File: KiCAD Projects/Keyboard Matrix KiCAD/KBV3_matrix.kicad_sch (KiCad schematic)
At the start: 100 parts, among them J1 Conn_01x06, U2 TCA8418RTWR

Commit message: Added a parts list summary with current prices for easier BOM Assembly
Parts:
- added J2: Conn_01x10_Socket, Connector_FFC-FPC:Molex_200528-0100_1x10-1MP_P1.00mm_Horizontal, symbol Connector:Conn_01x10_Socket

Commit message: Added RGB LED to the keypad matrix
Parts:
- removed J1: Conn_01x06, symbol Connector_Generic:Conn_01x06
- added C3: 0.1uF, symbol Device:C_Polarized_Small_US
- added LED1, LED10, LED11, LED12, LED13, LED14, LED15, LED16, LED17, LED18, LED19, LED2, LED20, LED21, LED22, LED23, LED24, LED25, LED26, LED27, LED28, LED29, LED3, LED30, LED31, LED32, LED33, LED34, LED35, LED36, LED37, LED38, LED39, LED4, LED40, LED41, LED42, LED43, LED44, LED45, LED46, LED47, LED48, LED5, LED6, LED7, LED8, LED9: PI554FCH, LED_SMD:LED_Inolux_IN-PI554FCH_PLCC4_5.0x5.0mm_P3.2mm, symbol LED:Inolux_IN-PI554FCH
- added R1: 500, symbol Device:R_US
- added R2: 10k, symbol Device:R_US
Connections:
- net +3.3V: now also J2.2 (Pin_2)
- net GND: now also J2.10 (Pin_10), C3.2, LED1.1 (VSS), LED10.1 (VSS), LED11.1 (VSS), LED12.1 (VSS), LED13.1 (VSS), LED14.1 (VSS), LED15.1 (VSS), LED16.1 (VSS), LED17.1 (VSS), LED18.1 (VSS), LED19.1 (VSS), LED2.1 (VSS), LED20.1 (VSS), LED21.1 (VSS), LED22.1 (VSS), LED23.1 (VSS), LED24.1 (VSS), LED25.1 (VSS), LED26.1 (VSS), LED27.1 (VSS), LED28.1 (VSS), LED29.1 (VSS), LED3.1 (VSS), LED30.1 (VSS), LED31.1 (VSS), LED32.1 (VSS), LED33.1 (VSS), LED34.1 (VSS), LED35.1 (VSS), LED36.1 (VSS), LED37.1 (VSS), LED38.1 (VSS), LED39.1 (VSS), LED4.1 (VSS), LED40.1 (VSS), LED41.1 (VSS), LED42.1 (VSS), LED43.1 (VSS), LED44.1 (VSS), LED45.1 (VSS), LED46.1 (VSS), LED47.1 (VSS), LED48.1 (VSS), LED5.1 (VSS), LED6.1 (VSS), LED7.1 (VSS), LED8.1 (VSS), LED9.1 (VSS), R2.2
- net INTn: now also J2.5 (Pin_5)
- net RESETn: now also J2.6 (Pin_6)
- net SCL: now also J2.3 (Pin_3)
- net SDA: now also J2.4 (Pin_4)
- net +5V: now reaches J2.1 (Pin_1)
- net +5V: now also C3.1, LED1.3 (VDD), LED10.3 (VDD), LED11.3 (VDD), LED12.3 (VDD), LED13.3 (VDD), LED14.3 (VDD), LED15.3 (VDD), LED16.3 (VDD), LED17.3 (VDD), LED18.3 (VDD), LED19.3 (VDD), LED2.3 (VDD), LED20.3 (VDD), LED21.3 (VDD), LED22.3 (VDD), LED23.3 (VDD), LED24.3 (VDD), LED25.3 (VDD), LED26.3 (VDD), LED27.3 (VDD), LED28.3 (VDD), LED29.3 (VDD), LED3.3 (VDD), LED30.3 (VDD), LED31.3 (VDD), LED32.3 (VDD), LED33.3 (VDD), LED34.3 (VDD), LED35.3 (VDD), LED36.3 (VDD), LED37.3 (VDD), LED38.3 (VDD), LED39.3 (VDD), LED4.3 (VDD), LED40.3 (VDD), LED41.3 (VDD), LED42.3 (VDD), LED43.3 (VDD), LED44.3 (VDD), LED45.3 (VDD), LED46.3 (VDD), LED47.3 (VDD), LED48.3 (VDD), LED5.3 (VDD), LED6.3 (VDD), LED7.3 (VDD), LED8.3 (VDD), LED9.3 (VDD)
- net LED Din: now reaches J2.8 (Pin_8)
- net LED Din: now also R1.1
- new net: LED37.4 (DO), LED38.2 (DIN)
- new net: LED16.4 (DO), LED17.2 (DIN)
- new net: LED17.4 (DO), LED18.2 (DIN)
- new net: LED29.4 (DO), LED30.2 (DIN)
- new net: LED30.4 (DO), LED31.2 (DIN)
- new net: LED10.4 (DO), LED11.2 (DIN)
- new net: LED11.4 (DO), LED12.2 (DIN)
- new net: LED13.4 (DO), LED14.2 (DIN)
- new net: LED14.4 (DO), LED15.2 (DIN)
- new net: LED4.4 (DO), LED5.2 (DIN)
- new net: LED5.4 (DO), LED6.2 (DIN)
- new net: LED15.4 (DO), LED16.2 (DIN)
- new net: LED48.4 (DO), R2.1
- new net: LED33.4 (DO), LED34.2 (DIN)
- new net: LED34.4 (DO), LED35.2 (DIN)
- new net: LED42.4 (DO), LED43.2 (DIN)
- new net: LED43.4 (DO), LED44.2 (DIN)
- new net: LED2.4 (DO), LED3.2 (DIN)
- new net: LED3.4 (DO), LED4.2 (DIN)
- new net: LED35.4 (DO), LED36.2 (DIN)
- new net: LED38.4 (DO), LED39.2 (DIN)
- new net: LED39.4 (DO), LED40.2 (DIN)
- new net: LED23.4 (DO), LED24.2 (DIN)
- new net: LED47.4 (DO), LED48.2 (DIN)
- new net: LED6.4 (DO), LED7.2 (DIN)
- new net: LED7.4 (DO), LED8.2 (DIN)
- new net: LED46.4 (DO), LED47.2 (DIN)
- new net: LED32.4 (DO), LED33.2 (DIN)
- new net: LED31.4 (DO), LED32.2 (DIN)
- new net: LED20.4 (DO), LED21.2 (DIN)
- new net: LED21.4 (DO), LED22.2 (DIN)
- new net: LED22.4 (DO), LED23.2 (DIN)
- new net: LED25.4 (DO), LED26.2 (DIN)
- new net: LED8.4 (DO), LED9.2 (DIN)
- new net: LED26.4 (DO), LED27.2 (DIN)
- new net: LED27.4 (DO), LED28.2 (DIN)
- new net: LED41.4 (DO), LED42.2 (DIN)
- new net: LED1.2 (DIN), R1.2
- new net: LED1.4 (DO), LED2.2 (DIN)
- new net: LED28.4 (DO), LED29.2 (DIN)
- new net: LED18.4 (DO), LED19.2 (DIN)
- new net: LED44.4 (DO), LED45.2 (DIN)
- new net: LED40.4 (DO), LED41.2 (DIN)
- new net: LED45.4 (DO), LED46.2 (DIN)
- new net: LED19.4 (DO), LED20.2 (DIN)
- new net: LED10.2 (DIN), LED9.4 (DO)
- new net LED Din R2: LED12.4 (DO), LED13.2 (DIN)
- new net LED Din R3: LED24.4 (DO), LED25.2 (DIN)
- new net LED Din R4: LED36.4 (DO), LED37.2 (DIN)
- no-connect marks 2 -> 0
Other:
- moved on the sheet: J2

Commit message: Clean Libraries, Added Datasheet, LDO, etc
Cleaned up some of the footprints that are not needed. Added components for PD and voltage regulation. Only minor changes to schematic
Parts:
- added H1, H2, H3, H4: MountingHole_Pad, symbol Mechanical:MountingHole_Pad
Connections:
- net GND: now also H1.1, H2.1, H3.1, H4.1

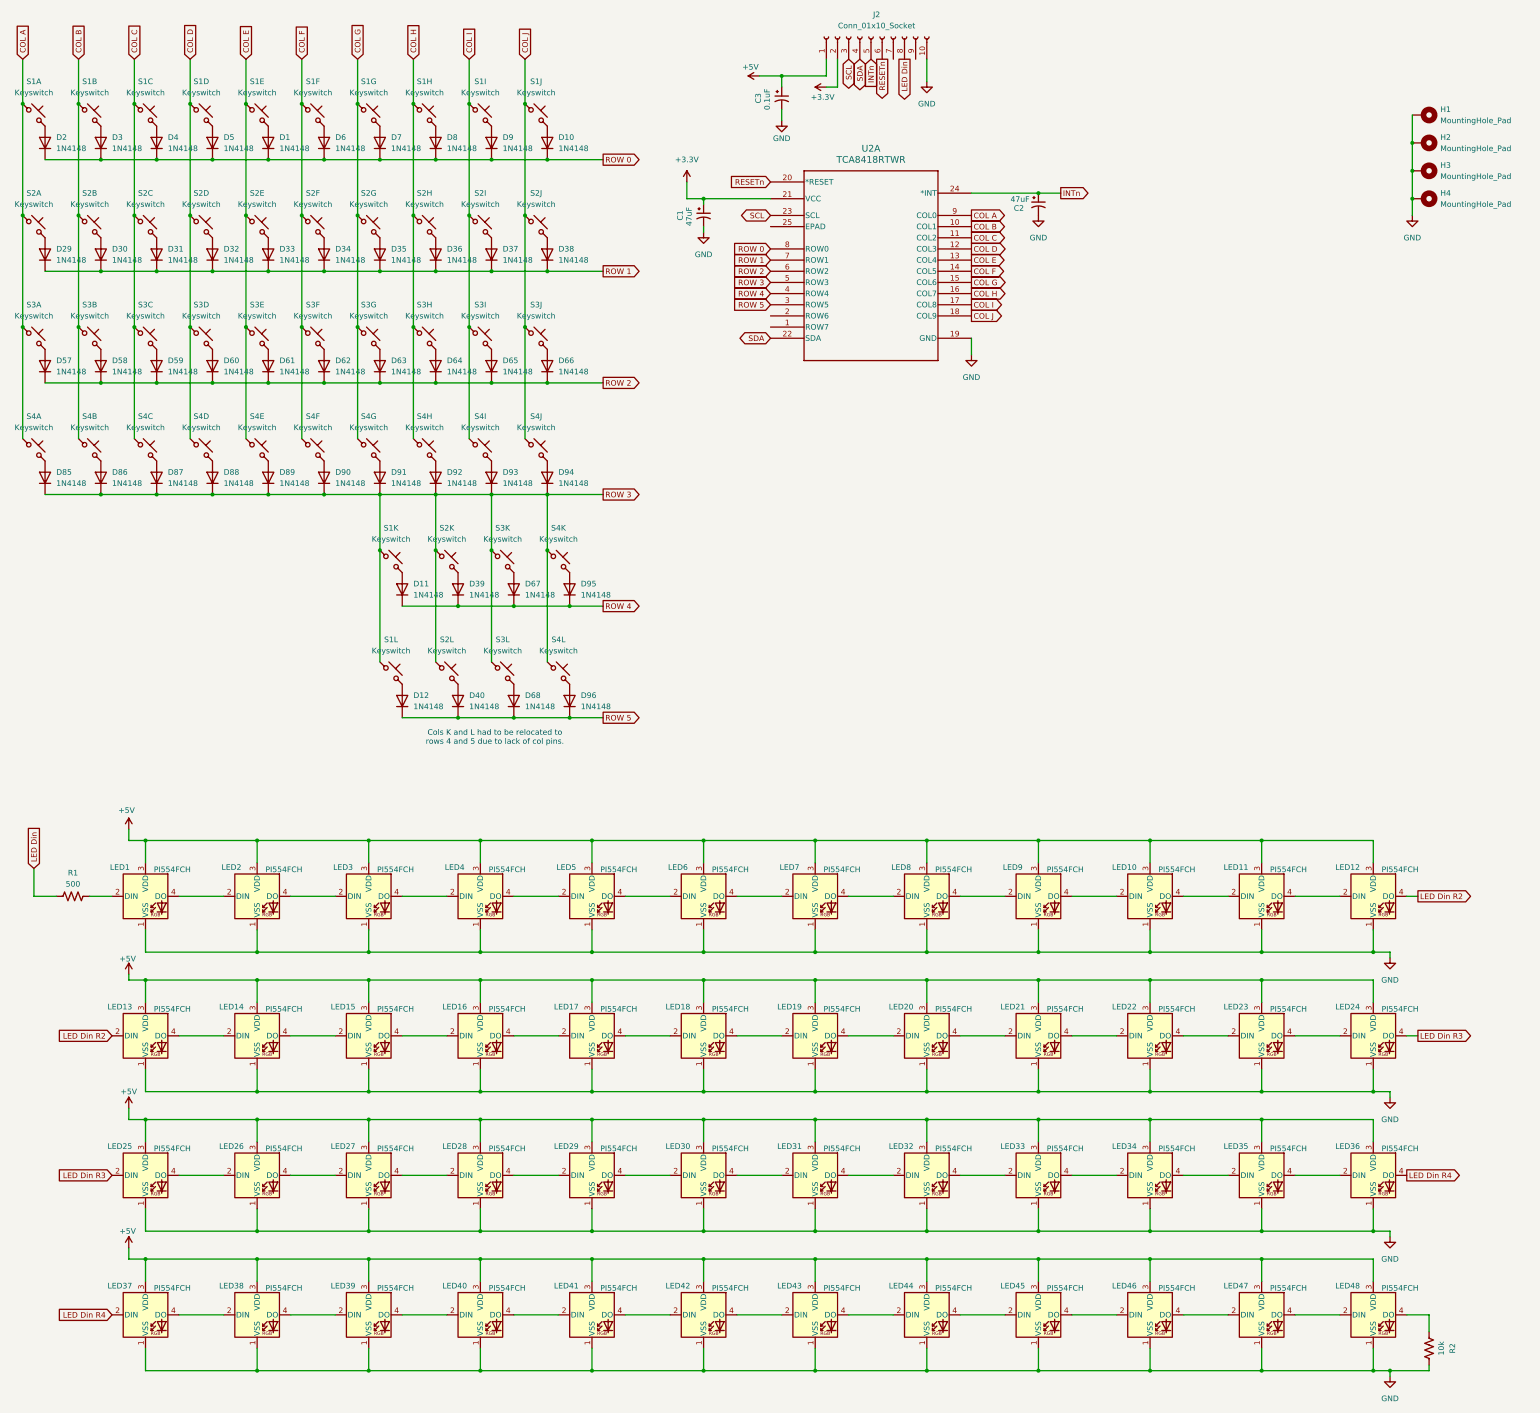
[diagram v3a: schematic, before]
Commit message: Changed the key matrix to one row 6 instead of two smaller rows.  Added USB ESD protection
Changed the key matrix to one row 6 instead of two smaller rows.

Added USB ESD protection
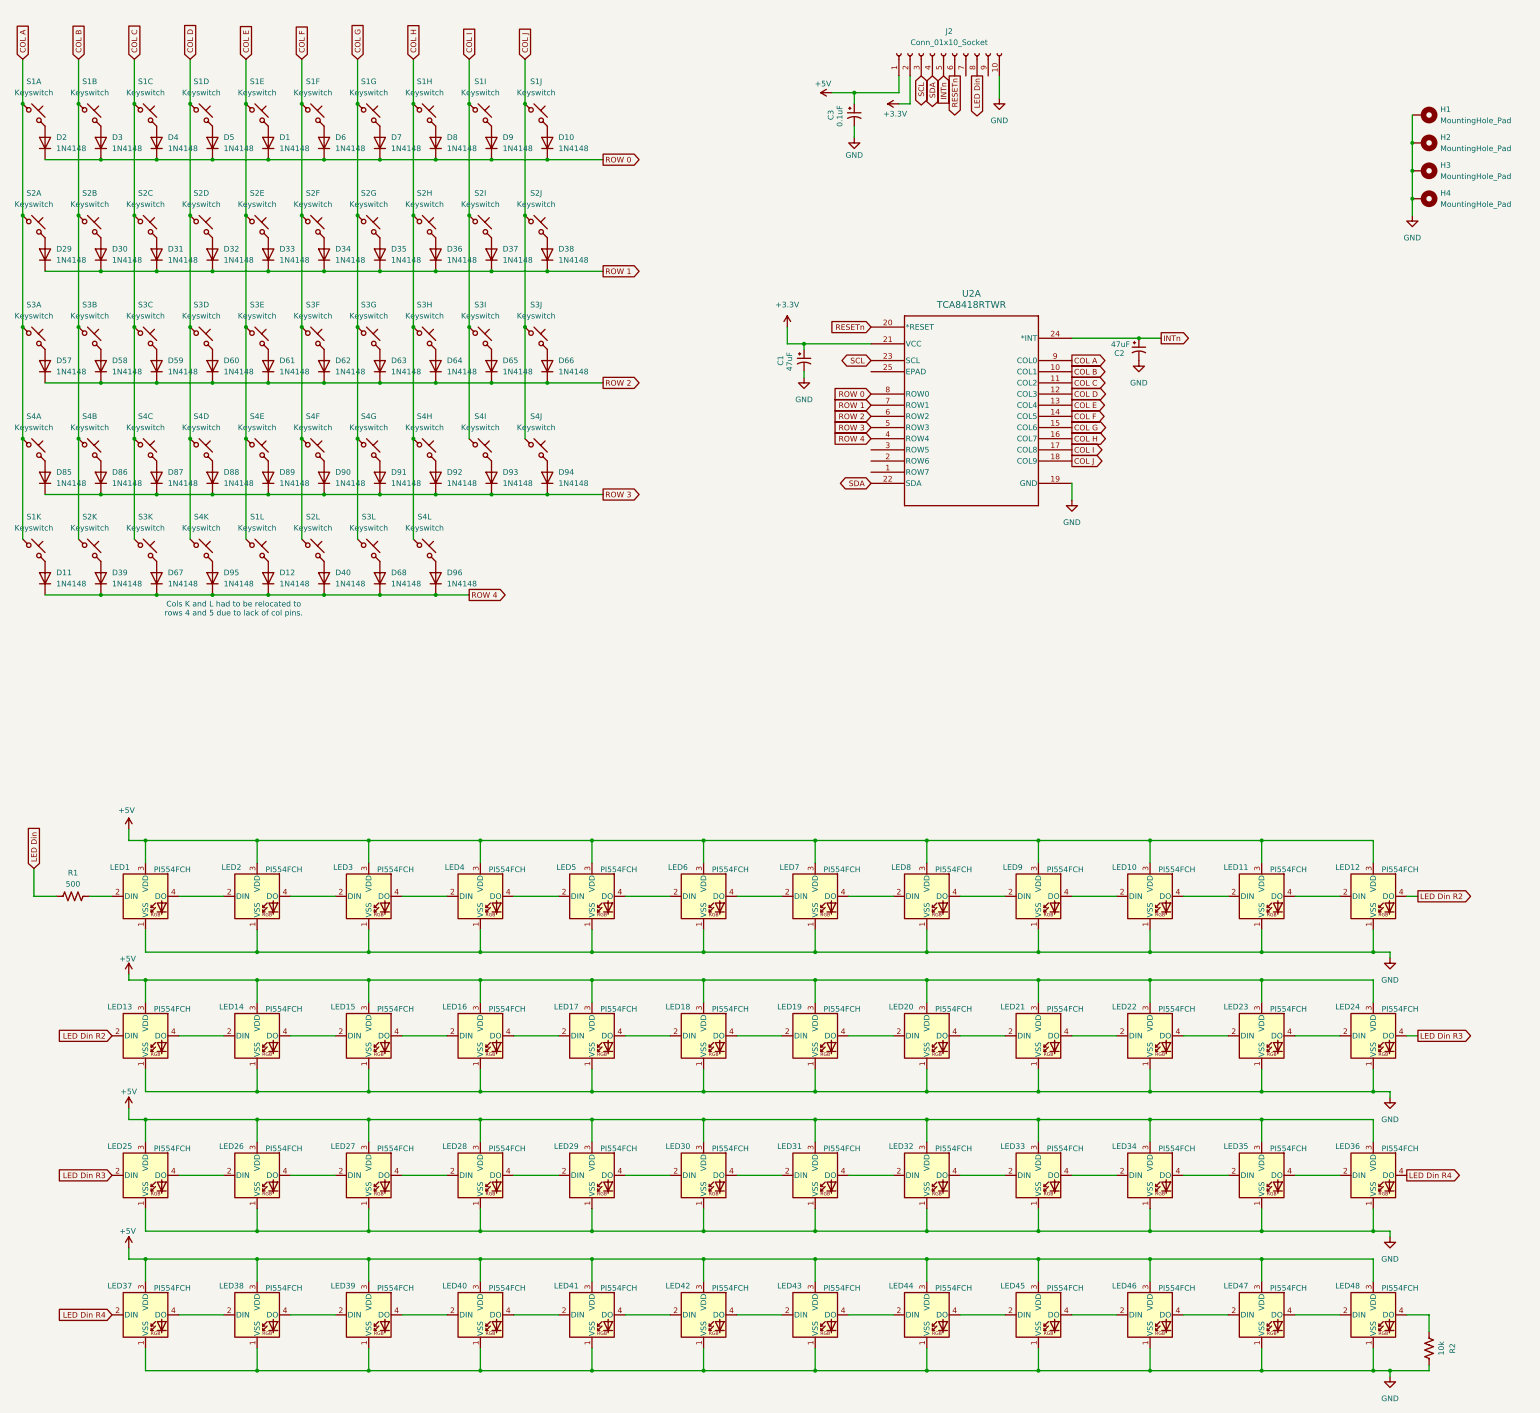
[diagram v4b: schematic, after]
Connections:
- net COL A: now also S1K.1
- net COL B: now also S2K.1
- net COL C: now also S3K.1
- net COL D: now also S4K.1
- net COL E: now also S1L.1
- net COL F: now also S2L.1
- net COL G: now also S3L.1
- net COL H: now also S4L.1
- net ROW 3: no longer S1K.1, S1L.1, S2K.1, S2L.1, S3K.1, S3L.1, S4K.1, S4L.1
- net ROW 4: now also D12.1 (K), D40.1 (K), D68.1 (K), D96.1 (K)
- removed net ROW 5: D12.1 (K), D40.1 (K), D68.1 (K), D96.1 (K), U2.3 (ROW5)
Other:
- moved on the sheet: C1, C2, C3, D11, D12, D39, D40, D67, D68, D95, D96, J2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
